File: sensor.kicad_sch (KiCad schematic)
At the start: 4 parts, among them U2 SLSS49E-3

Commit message: add reverse polarity protection to LDO
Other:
- title: (none) -> MoonBoard
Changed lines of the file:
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@@
 (kicad_sch (version 20230121) (generator eeschema)
   (paper "A5")
+  (title_block
+    (title "MoonBoard")
+  )
   (junction (at 99.695 60.325) (diameter 0) (color 0 0 0 0)
   )

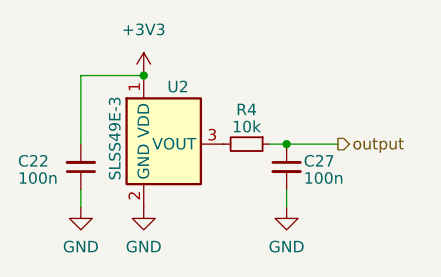
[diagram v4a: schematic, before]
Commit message: update to kicad 8
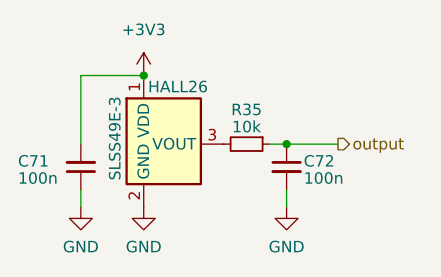
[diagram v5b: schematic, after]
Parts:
- renumbered C22 to C71, C27 to C72, U2 to HALL26, R4 to R35
